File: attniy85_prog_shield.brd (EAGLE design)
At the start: 68.6 x 53.3 mm, 2 parts, among them U1 ARDUINOR3-BPLACE

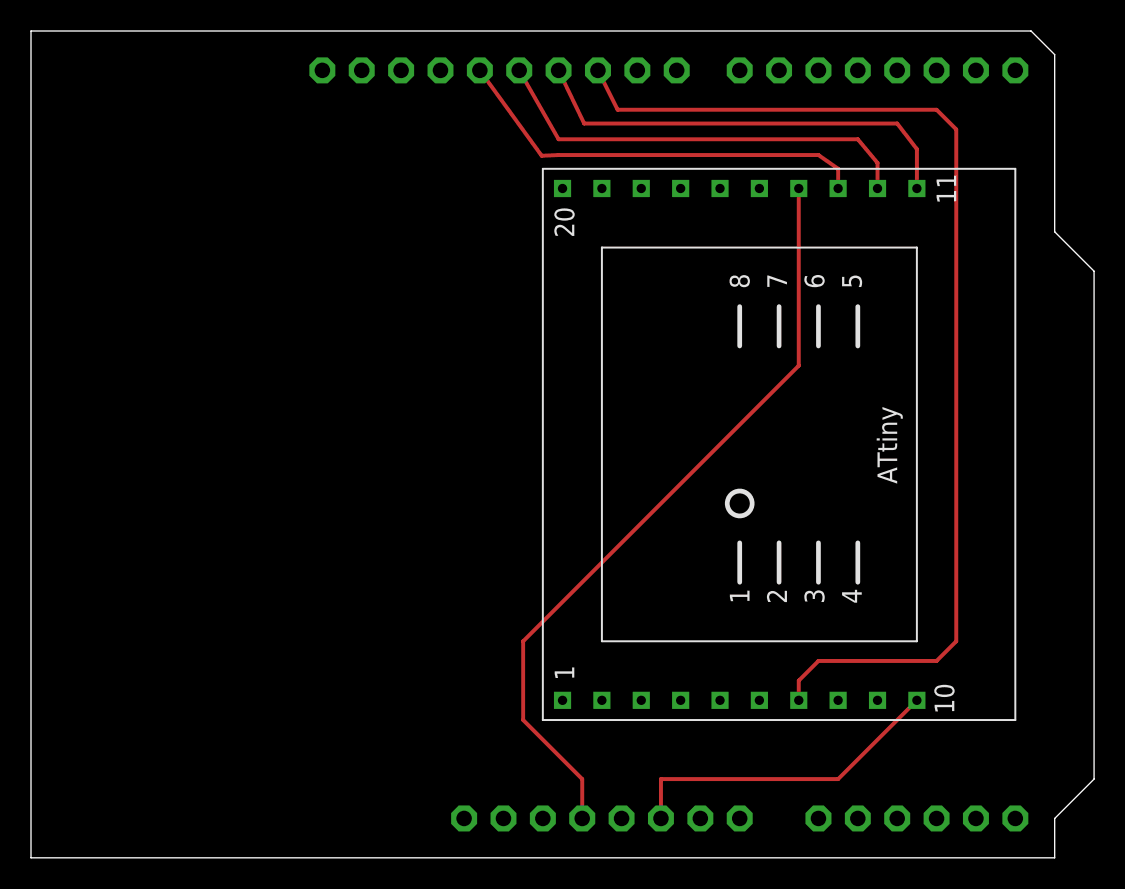
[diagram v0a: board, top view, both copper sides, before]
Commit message: correct zif width
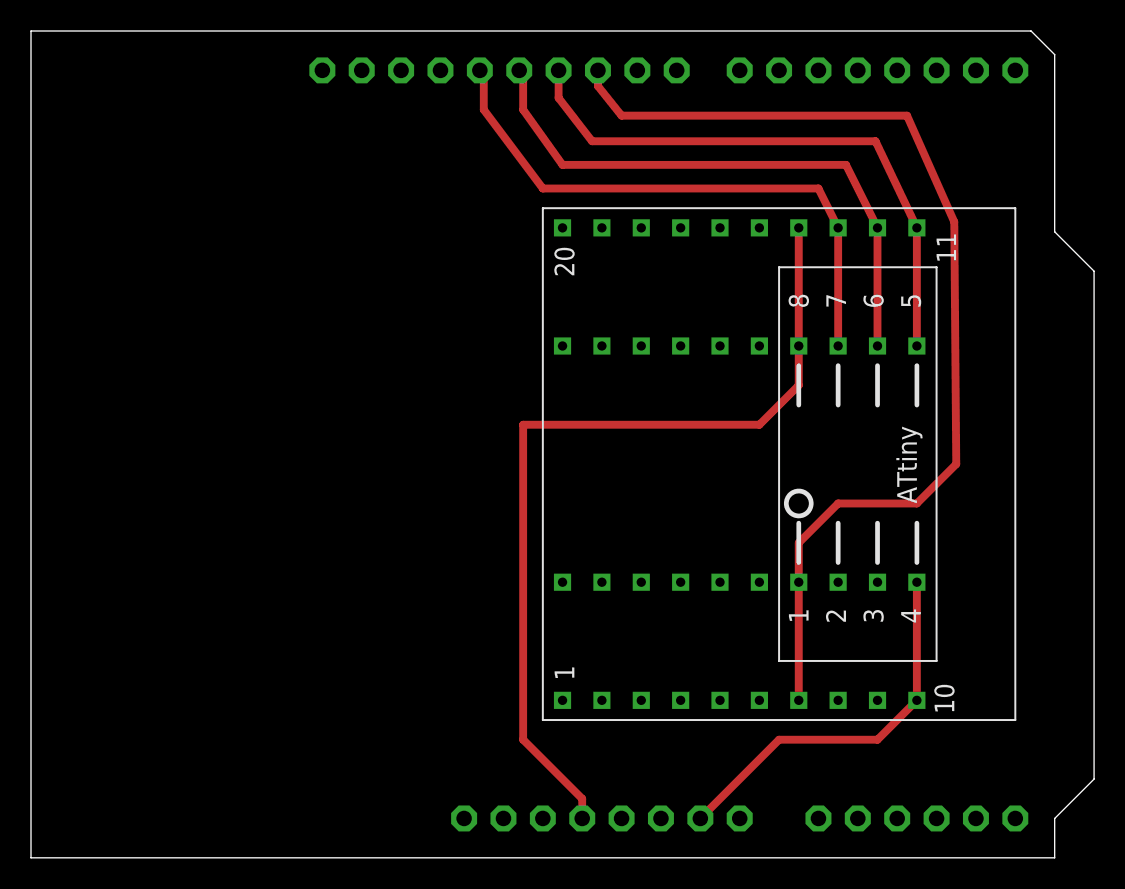
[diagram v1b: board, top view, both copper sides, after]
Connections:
- net GND: now also U$1.P$30
- net MISO: now also U$1.P$32
- net MOSI: now also U$1.P$31
- net NC: now also U$1.P$28, U$1.P$29
- net RESET: now also U$1.P$27
- net SCK: now also U$1.P$33
- net VCC: now also U$1.P$34
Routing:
- net SCK: track 27.5 -> 37.2 mm
- net MISO: track 28.1 -> 37.5 mm
- net MOSI: track 28.6 -> 37.4 mm
- net VCC: track 49.6 -> 56.0 mm
- net GND: track 21.2 -> 24.7 mm
- net RESET: track 70.7 -> 67.4 mm
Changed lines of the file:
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@@
 <setting verticaltext="up"/>
 </settings>
-<grid distance="50" unitdist="mil" unit="mil" style="lines" multiple="5" display="yes" altdistance="5" altunitdist="mil" altunit="mil"/>
+<grid distance="5" unitdist="mil" unit="mil" style="lines" multiple="5" display="yes" altdistance="5" altunitdist="mil" altunit="mil"/>
 <layers>
 <layer number="1" name="Top" color="4" fill="1" visible="yes" active="yes"/>
@@
 <layer number="17" name="Pads" color="2" fill="1" visible="yes" active="yes"/>
 <layer number="18" name="Vias" color="2" fill="1" visible="yes" active="yes"/>
-<layer number="19" name="Unrouted" color="6" fill="1" visible="no" active="yes"/>
+<layer number="19" name="Unrouted" color="6" fill="1" visible="yes" active="yes"/>
 <layer number="20" name="Dimension" color="15" fill="1" visible="yes" active="yes"/>
-<layer number="21" name="tPlace" color="16" fill="1" visible="no" active="yes"/>
+<layer number="21" name="tPlace" color="16" fill="1" visible="yes" active="yes"/>
 <layer number="22" name="bPlace" color="14" fill="1" visible="no" active="yes"/>
-<layer number="23" name="tOrigins" color="15" fill="1" visible="no" active="yes"/>
+<layer number="23" name="tOrigins" color="15" fill="1" visible="yes" active="yes"/>
 <layer number="24" name="bOrigins" color="15" fill="1" visible="no" active="yes"/>
-<layer number="25" name="tNames" color="7" fill="1" visible="no" active="yes"/>
+<layer number="25" name="tNames" color="7" fill="1" visible="yes" active="yes"/>
 <layer number="26" name="bNames" color="7" fill="1" visible="no" active="yes"/>
 <layer number="27" name="tValues" color="7" fill="1" visible="no" active="yes"/>
@@
 <layer number="37" name="tTest" color="13" fill="1" visible="no" active="yes"/>
 <layer number="38" name="bTest" color="7" fill="1" visible="no" active="yes"/>
-<layer number="39" name="tKeepout" color="4" fill="11" visible="no" active="yes"/>
+<layer number="39" name="tKeepout" color="4" fill="11" visible="yes" active="yes"/>
 <layer number="40" name="bKeepout" color="1" fill="11" visible="no" active="yes"/>
-<layer number="41" name="tRestrict" color="4" fill="10" visible="no" active="yes"/>
+<layer number="41" name="tRestrict" color="4" fill="10" visible="yes" active="yes"/>
 <layer number="42" name="bRestrict" color="1" fill="10" visible="no" active="yes"/>
 <layer number="43" name="vRestrict" color="2" fill="10" visible="no" active="yes"/>
 <layer number="44" name="Drills" color="7" fill="1" visible="no" active="yes"/>
-<layer number="45" name="Holes" color="7" fill="1" visible="no" active="yes"/>
+<layer number="45" name="Holes" color="7" fill="1" visible="yes" active="yes"/>
 <layer number="46" name="Milling" color="3" fill="1" visible="no" active="yes"/>
 <layer number="47" name="Measures" color="7" fill="1" visible="no" active="yes"/>
@@
 <layer number="49" name="Reference" color="7" fill="1" visible="no" active="yes"/>
 <layer number="50" name="dxf" color="7" fill="1" visible="no" active="no"/>
-<layer number="51" name="tDocu" color="6" fill="1" visible="no" active="yes"/>
+<layer number="51" name="tDocu" color="6" fill="1" visible="yes" active="yes"/>
 <layer number="52" name="bDocu" color="7" fill="1" visible="no" active="yes"/>
 <layer number="53" name="tGND_GNDA" color="7" fill="9" visible="no" active="no"/>
@@
 <contactref element="U1" pad="GND1"/>
 <contactref element="U$1" pad="P$10"/>
-<wire x1="52.07" y1="5.08" x2="40.64" y2="5.08" width="0.254" layer="1"/>
-<wire x1="40.64" y1="5.08" x2="40.64" y2="2.54" width="0.254" layer="1"/>
-<wire x1="57.15" y1="10.16" x2="52.07" y2="5.08" width="0.254" layer="1"/>
-<wire x1="40.64" y1="5.08" x2="26.416" y2="50.8" width="0" layer="19" extent="1-1"/>
-<wire x1="43.18" y1="2.54" x2="40.64" y2="2.54" width="0" layer="19" extent="1-1"/>
+<wire x1="43.18" y1="2.54" x2="48.26" y2="7.62" width="0.508" layer="1"/>
+<wire x1="48.26" y1="7.62" x2="54.61" y2="7.62" width="0.508" layer="1"/>
+<wire x1="54.61" y1="7.62" x2="57.15" y2="10.16" width="0.508" layer="1"/>
+<contactref element="U$1" pad="P$30"/>
+<wire x1="57.15" y1="17.78" x2="57.15" y2="10.16" width="0.508" layer="1"/>
+<wire x1="57.15" y1="17.78" x2="26.416" y2="50.8" width="0" layer="19" extent="1-1"/>
+<wire x1="40.64" y1="2.54" x2="43.18" y2="2.54" width="0" layer="19" extent="1-1"/>
 </signal>
 <signal name="VIN">
@@
 <contactref element="U$1" pad="P$14"/>
 <contactref element="U1" pad="3V"/>
-<wire x1="49.53" y1="43.18" x2="49.53" y2="31.75" width="0.254" layer="1"/>
-<wire x1="49.53" y1="31.75" x2="31.75" y2="13.97" width="0.254" layer="1"/>
-<wire x1="31.75" y1="13.97" x2="31.75" y2="8.89" width="0.254" layer="1"/>
-<wire x1="31.75" y1="8.89" x2="35.56" y2="5.08" width="0.254" layer="1"/>
-<wire x1="35.56" y1="5.08" x2="35.56" y2="2.54" width="0.254" layer="1"/>
+<contactref element="U$1" pad="P$34"/>
+<wire x1="49.53" y1="40.64" x2="49.53" y2="33.02" width="0.508" layer="1"/>
+<wire x1="49.53" y1="33.02" x2="49.53" y2="30.48" width="0.508" layer="1"/>
+<wire x1="49.53" y1="30.48" x2="46.99" y2="27.94" width="0.508" layer="1"/>
+<wire x1="46.99" y1="27.94" x2="31.75" y2="27.94" width="0.508" layer="1"/>
+<wire x1="31.75" y1="27.94" x2="31.75" y2="7.62" width="0.508" layer="1"/>
+<wire x1="35.56" y1="3.81" x2="35.56" y2="2.54" width="0.508" layer="1"/>
+<wire x1="31.75" y1="7.62" x2="35.56" y2="3.81" width="0.508" layer="1"/>
 </signal>
 <signal name="SCK">
 <contactref element="U1" pad="D13"/>
 <contactref element="U$1" pad="P$13"/>
-<wire x1="28.956" y1="50.8" x2="32.947828125" y2="45.289584375" width="0.254" layer="1"/>
-<wire x1="32.947828125" y1="45.289584375" x2="34.036" y2="45.339" width="0.254" layer="1"/>
-<wire x1="34.036" y1="45.339" x2="50.8" y2="45.339" width="0.254" layer="1"/>
-<wire x1="50.8" y1="45.339" x2="52.07" y2="44.45" width="0.254" layer="1"/>
-<wire x1="52.07" y1="44.45" x2="52.07" y2="43.18" width="0.254" layer="1"/>
+<wire x1="28.956" y1="50.8" x2="29.21" y2="50.546" width="0.508" layer="1"/>
+<wire x1="29.21" y1="50.546" x2="29.21" y2="48.26" width="0.508" layer="1"/>
+<wire x1="29.21" y1="48.26" x2="33.02" y2="43.18" width="0.508" layer="1"/>
+<wire x1="33.02" y1="43.18" x2="50.8" y2="43.18" width="0.508" layer="1"/>
+<wire x1="50.8" y1="43.18" x2="52.07" y2="40.64" width="0.508" layer="1"/>
+<contactref element="U$1" pad="P$33"/>
+<wire x1="52.07" y1="40.64" x2="52.07" y2="33.02" width="0.508" layer="1"/>
 </signal>
 <signal name="MISO">
 <contactref element="U1" pad="D12"/>
 <contactref element="U$1" pad="P$12"/>
-<wire x1="31.496" y1="50.8" x2="34.036" y2="46.355" width="0.254" layer="1"/>
-<wire x1="34.036" y1="46.355" x2="53.34" y2="46.355" width="0.254" layer="1"/>
-<wire x1="53.34" y1="46.355" x2="54.61" y2="44.831" width="0.254" layer="1"/>
-<wire x1="54.61" y1="44.831" x2="54.61" y2="43.18" width="0.254" layer="1"/>
+<wire x1="31.496" y1="50.8" x2="31.75" y2="50.546" width="0.508" layer="1"/>
+<wire x1="31.75" y1="50.546" x2="31.75" y2="48.26" width="0.508" layer="1"/>
+<wire x1="31.75" y1="48.26" x2="34.29" y2="44.704" width="0.508" layer="1"/>
+<wire x1="34.29" y1="44.704" x2="52.578" y2="44.704" width="0.508" layer="1"/>
+<wire x1="52.578" y1="44.704" x2="54.61" y2="40.64" width="0.508" layer="1"/>
+<contactref element="U$1" pad="P$32"/>
+<wire x1="54.61" y1="40.64" x2="54.61" y2="33.02" width="0.508" layer="1"/>
 </signal>
 <signal name="MOSI">
 <contactref element="U1" pad="D11"/>
 <contactref element="U$1" pad="P$11"/>
-<wire x1="34.036" y1="50.8" x2="35.687" y2="47.371" width="0.254" layer="1"/>
-<wire x1="35.687" y1="47.371" x2="55.88" y2="47.371" width="0.254" layer="1"/>
-<wire x1="55.88" y1="47.371" x2="57.15" y2="45.72" width="0.254" layer="1"/>
-<wire x1="57.15" y1="45.72" x2="57.15" y2="43.18" width="0.254" layer="1"/>
+<wire x1="34.036" y1="50.8" x2="34.036" y2="49.022" width="0.508" layer="1"/>
+<wire x1="36.195" y1="46.228" x2="54.483" y2="46.228" width="0.508" layer="1"/>
+<wire x1="54.483" y1="46.228" x2="57.15" y2="40.64" width="0.508" layer="1"/>
+<wire x1="34.036" y1="49.022" x2="36.195" y2="46.228" width="0.508" layer="1"/>
+<contactref element="U$1" pad="P$31"/>
+<wire x1="57.15" y1="40.64" x2="57.15" y2="33.02" width="0.508" layer="1"/>
 </signal>
 <signal name="RESET">
 <contactref element="U1" pad="D10"/>
 <contactref element="U$1" pad="P$7"/>
-<wire x1="36.576" y1="50.8" x2="37.846" y2="48.26" width="0.254" layer="1"/>
-<wire x1="37.846" y1="48.26" x2="58.42" y2="48.26" width="0.254" layer="1"/>
-<wire x1="58.42" y1="48.26" x2="59.69" y2="46.99" width="0.254" layer="1"/>
-<wire x1="59.69" y1="46.99" x2="59.69" y2="13.97" width="0.254" layer="1"/>
-<wire x1="59.69" y1="13.97" x2="58.42" y2="12.7" width="0.254" layer="1"/>
-<wire x1="58.42" y1="12.7" x2="50.8" y2="12.7" width="0.254" layer="1"/>
-<wire x1="50.8" y1="12.7" x2="49.53" y2="11.43" width="0.254" layer="1"/>
-<wire x1="49.53" y1="11.43" x2="49.53" y2="10.16" width="0.254" layer="1"/>
+<contactref element="U$1" pad="P$27"/>
+<wire x1="49.53" y1="17.78" x2="49.53" y2="10.16" width="0.508" layer="1"/>
+<wire x1="36.576" y1="50.8" x2="36.576" y2="49.784" width="0.508" layer="1"/>
+<wire x1="36.576" y1="49.784" x2="38.1" y2="47.879" width="0.508" layer="1"/>
+<wire x1="38.1" y1="47.879" x2="56.515" y2="47.879" width="0.508" layer="1"/>
+<wire x1="56.515" y1="47.879" x2="59.563" y2="41.021" width="0.508" layer="1"/>
+<wire x1="59.563" y1="41.021" x2="59.69" y2="25.4" width="0.508" layer="1"/>
+<wire x1="57.15" y1="22.86" x2="52.07" y2="22.86" width="0.508" layer="1"/>
+<wire x1="52.07" y1="22.86" x2="49.53" y2="20.32" width="0.508" layer="1"/>
+<wire x1="49.53" y1="20.32" x2="49.53" y2="17.78" width="0.508" layer="1"/>
+<wire x1="59.69" y1="25.4" x2="57.15" y2="22.86" width="0.508" layer="1"/>
 </signal>
 <signal name="5V">
@@
 <contactref element="U$1" pad="P$9"/>
 <wire x1="52.07" y1="10.16" x2="54.61" y2="10.16" width="0" layer="19" extent="1-1"/>
+<contactref element="U$1" pad="P$29"/>
+<contactref element="U$1" pad="P$28"/>
 </signal>
 </signals>
